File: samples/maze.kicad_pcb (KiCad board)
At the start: 2 copper layers, 20 x 20 mm, 0 parts

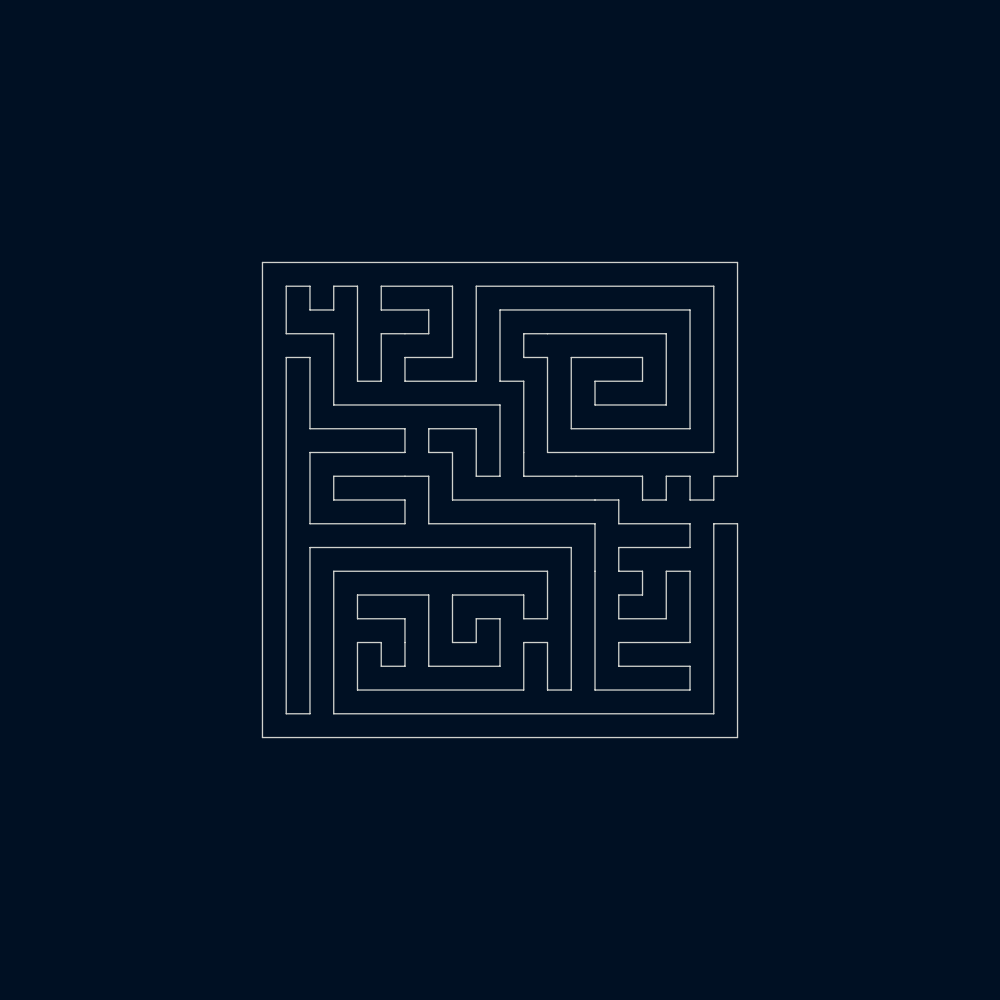
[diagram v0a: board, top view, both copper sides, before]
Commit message: update samples/{fpc,maze}
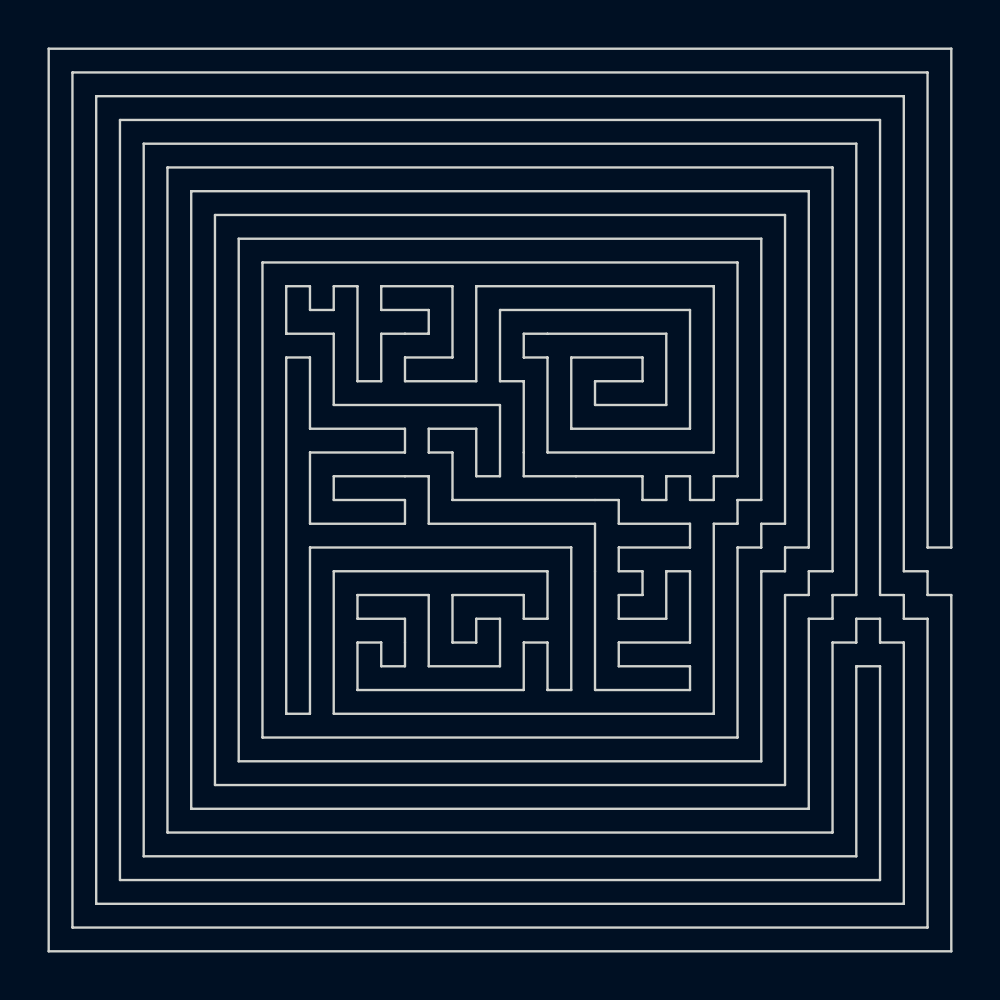
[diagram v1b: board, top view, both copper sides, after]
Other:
- board size 20 x 20 mm -> 38 x 38 mm
- board text added: "a=-30"
- board text added: "a=-30 r=1"
- board text added: "a=30"
- board text added: "a=30 r=1"

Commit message: update samples/{fpc.maze}
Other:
- board text added: "a=-30 r=0"
- board text added: "a=30 r=0"
- board text removed: "a=-30"
- board text removed: "a=-30 r=1"
- board text removed: "a=30"
- board text removed: "a=30 r=1"
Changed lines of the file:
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@@
 		(layer "User.4")
 	)
-	(gr_text "a=-30 r=1"
+	(gr_text "a=-30 r=0"
 		(at 101 130 270)
 		(layer "User.4")
@@
 		)
 	)
-	(gr_text "a=30 r=1"
+	(gr_text "a=30 r=0"
 		(at 104 130 270)
 		(layer "User.4")
@@
 		)
 	)
-	(gr_text "a=-30"
+	(gr_text "a=-30 r=0"
 		(at 107 130 270)
 		(layer "User.4")
@@
 		)
 	)
-	(gr_text "a=30"
+	(gr_text "a=30 r=0"
 		(at 110 130 270)
 		(layer "User.4")
@@
 		)
 	)
-	(gr_text "a=-30"
+	(gr_text "a=-30 r=0"
 		(at 113 130 270)
 		(layer "User.4")
@@
 		)
 	)
-	(gr_text "a=30"
+	(gr_text "a=30 r=0"
 		(at 116 130 270)
 		(layer "User.4")
@@
 		)
 	)
-	(gr_text "a=-30"
+	(gr_text "a=-30 r=0"
 		(at 119 130 270)
 		(layer "User.4")
